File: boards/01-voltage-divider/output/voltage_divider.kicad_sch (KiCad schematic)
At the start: 4 parts, among them J1 IN, J2 OUT

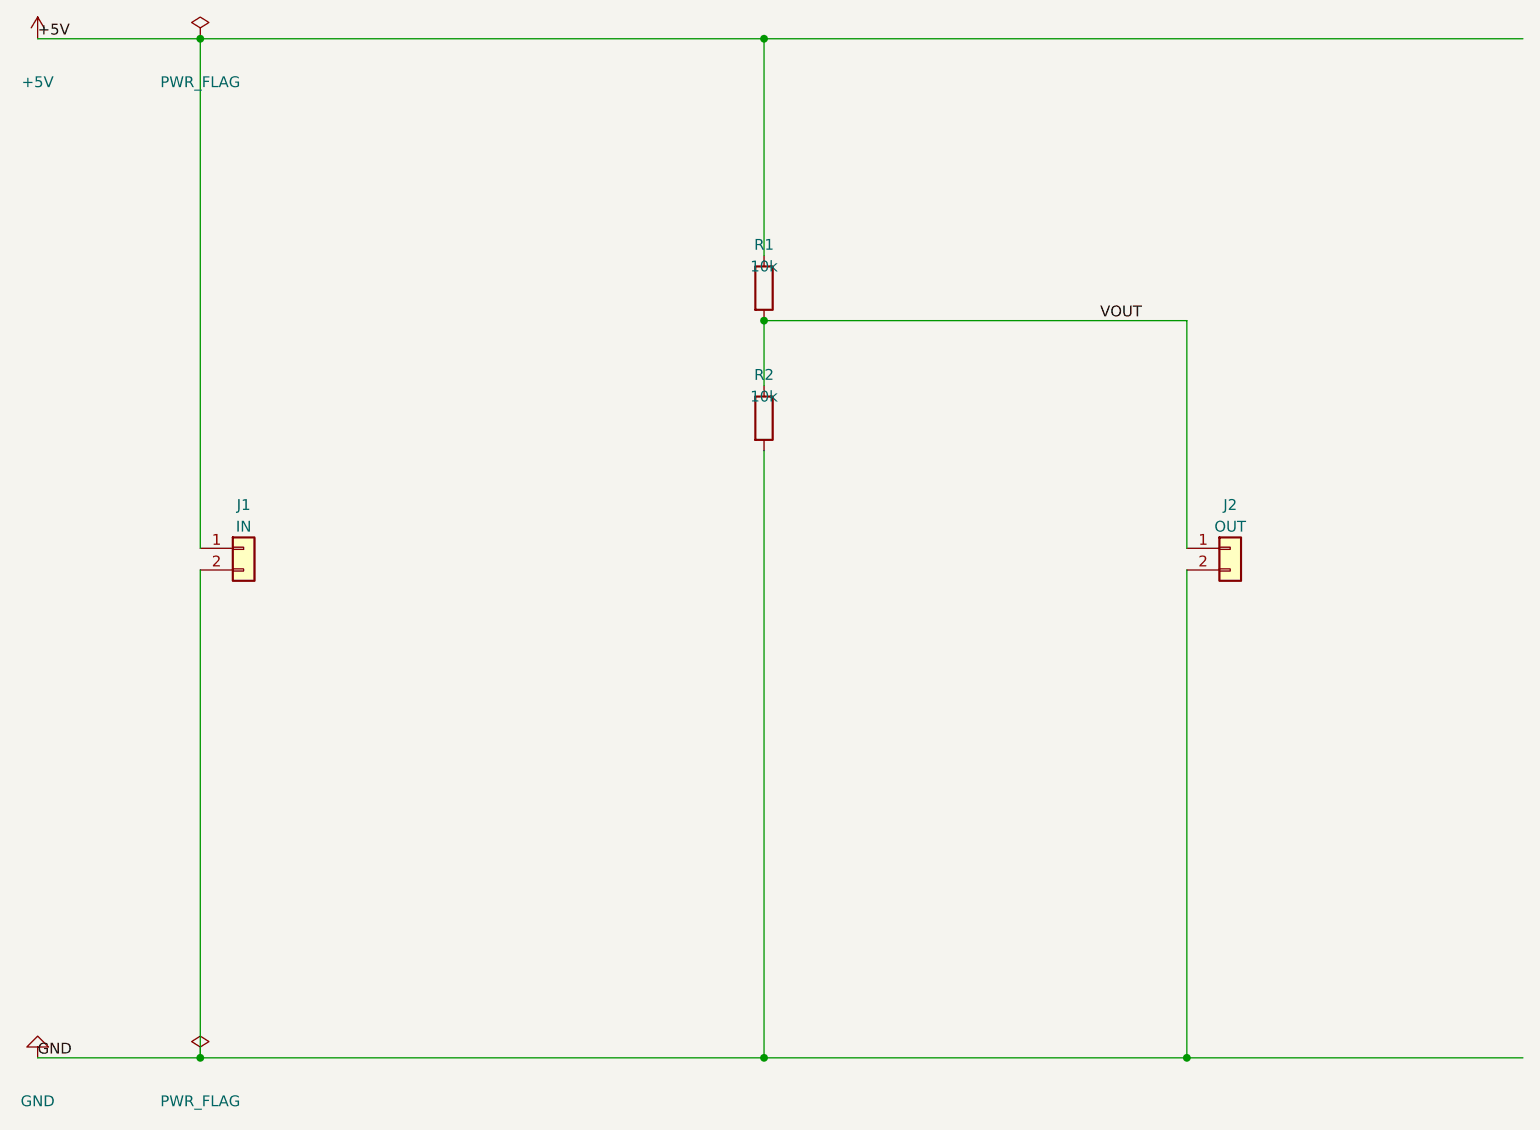
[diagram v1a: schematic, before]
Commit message: fix(boards): Add ERC validation to generate_design.py
The script previously reported SUCCESS even when the schematic had ERC
errors. Now runs KiCad ERC validation after schematic creation and:
- Reports ERC errors/warnings in the console output
- Includes ERC status in the summary (PASS/FAIL)
- Returns non-zero exit code when ERC errors are found
- Gracefully skips ERC if kicad-cli is not available

Co-Authored-By: Claude Opus 4.5 <noreply@anthropic.com>
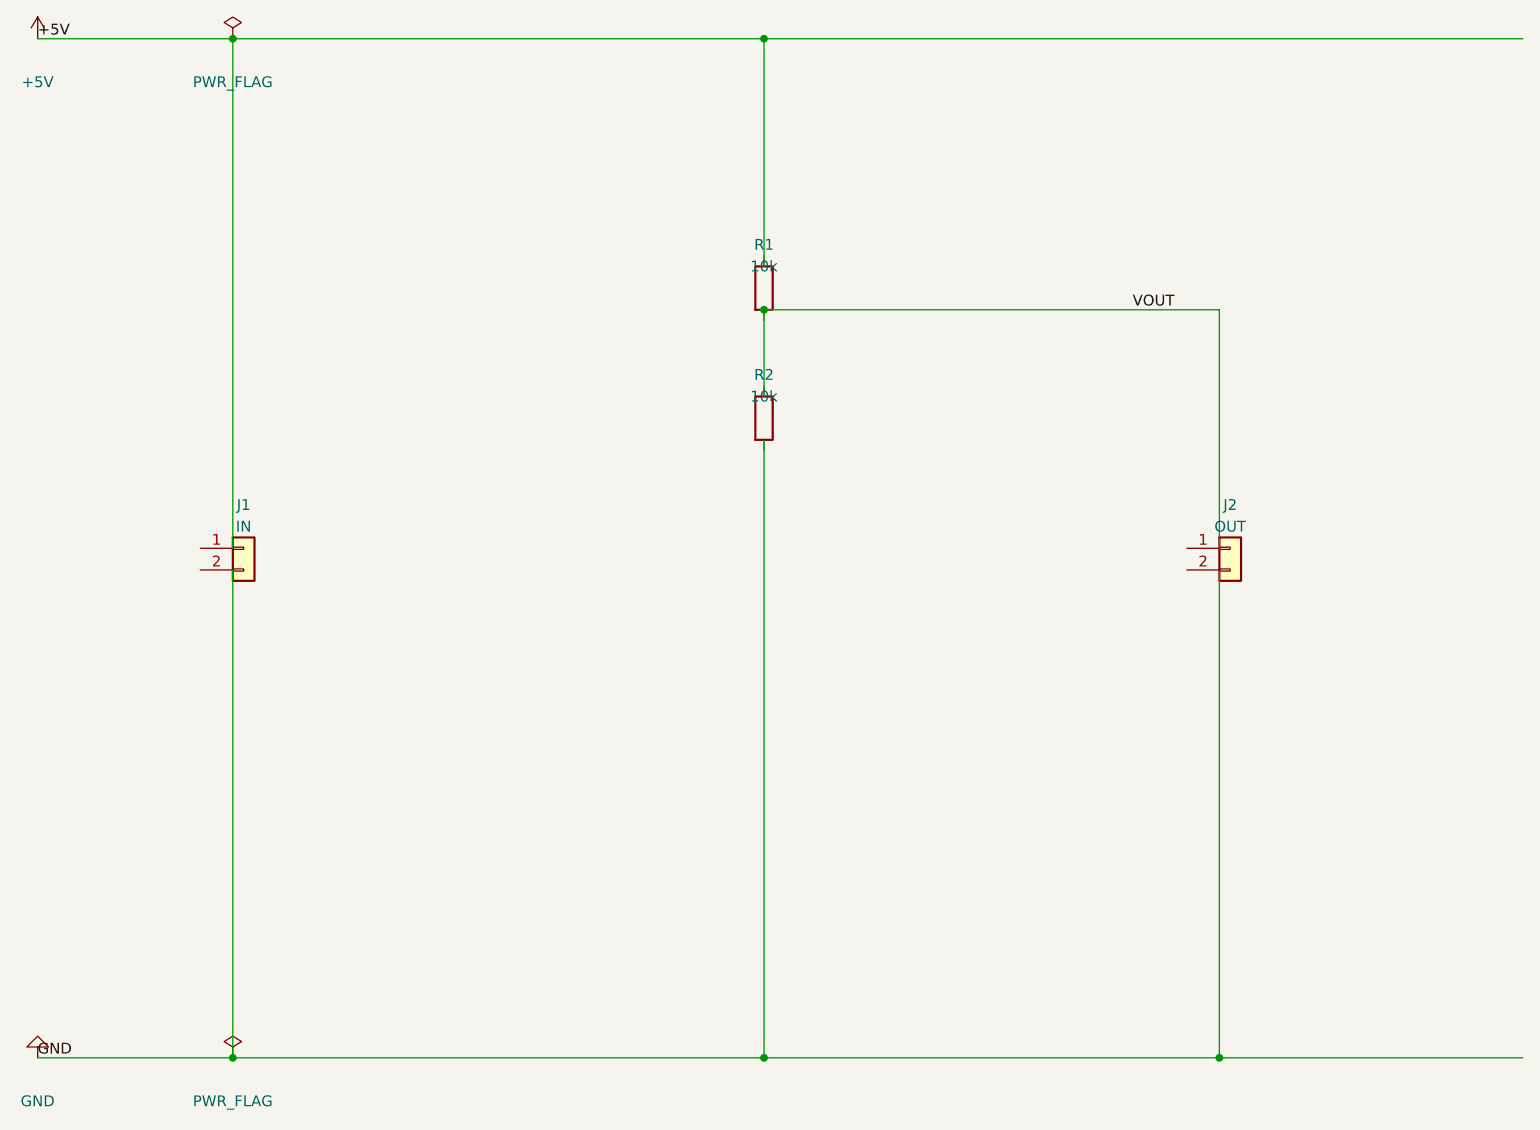
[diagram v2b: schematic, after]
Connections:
- net +5V: no longer J1.1 (Pin_1), R1.1
- net GND: no longer J1.2 (Pin_2), J2.2 (Pin_2), R2.2
- net VOUT: no longer J2.1 (Pin_1), R1.2, R2.1
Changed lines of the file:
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@@
     (instances
       (project "project"
-        (path "/9375341a-6719-4783-a821-5891f6b993f4" (reference "J1") (unit 1)
+        (path "/72230662-432b-4452-80bb-e7fa0bcafb7e" (reference "J1") (unit 1)
         )
       )
@@
     (instances
       (project "project"
-        (path "/9375341a-6719-4783-a821-5891f6b993f4" (reference "R1") (unit 1)
+        (path "/72230662-432b-4452-80bb-e7fa0bcafb7e" (reference "R1") (unit 1)
         )
       )
@@
     (instances
       (project "project"
-        (path "/9375341a-6719-4783-a821-5891f6b993f4" (reference "R2") (unit 1)
+        (path "/72230662-432b-4452-80bb-e7fa0bcafb7e" (reference "R2") (unit 1)
         )
       )
@@
     (instances
       (project "project"
-        (path "/9375341a-6719-4783-a821-5891f6b993f4" (reference "J2") (unit 1)
+        (path "/72230662-432b-4452-80bb-e7fa0bcafb7e" (reference "J2") (unit 1)
         )
       )
@@
     (instances
       (project "project"
-        (path "/9375341a-6719-4783-a821-5891f6b993f4" (reference "#PWR01") (unit 1)
+        (path "/72230662-432b-4452-80bb-e7fa0bcafb7e" (reference "#PWR01") (unit 1)
         )
       )
@@
     (instances
       (project "project"
-        (path "/9375341a-6719-4783-a821-5891f6b993f4" (reference "#PWR02") (unit 1)
+        (path "/72230662-432b-4452-80bb-e7fa0bcafb7e" (reference "#PWR02") (unit 1)
         )
       )
@@
   (symbol
     (lib_id "power:PWR_FLAG")
-    (at 44.45 30.48 0)
+    (at 48.26 30.48 0)
     (unit 1)
     (exclude_from_sim no)
@@
     (dnp no)
     (property "Reference" "#PWR03"
-      (at 44.45 33.02 0)
+      (at 48.26 33.02 0)
       (effects
         (font
@@
     )
     (property "Value" "PWR_FLAG"
-      (at 44.45 35.56 0)
-      (effects
-        (font
-          (size 1.27 1.27)
-        )
-      )
-    )
-    (property "Footprint" ""
-      (at 44.45 30.48 0)
+      (at 48.26 35.56 0)
+      (effects
+        (font
+          (size 1.27 1.27)
+        )
+      )
+    )
+    (property "Footprint" ""
+      (at 48.26 30.48 0)
       (effects
         (font
@@
     )
     (property "Datasheet" ""
-      (at 44.45 30.48 0)
-      (effects
-        (font
-          (size 1.27 1.27)
-        )
-        (hide yes)
-      )
-    )
-    (pin "1"
-    )
-    (instances
-      (project "project"
-        (path "/9375341a-6719-4783-a821-5891f6b993f4" (reference "#PWR03") (unit 1)
+      (at 48.26 30.48 0)
+      (effects
+        (font
+          (size 1.27 1.27)
+        )
+        (hide yes)
+      )
+    )
+    (pin "1"
+    )
+    (instances
+      (project "project"
+        (path "/72230662-432b-4452-80bb-e7fa0bcafb7e" (reference "#PWR03") (unit 1)
         )
       )
@@
   (symbol
     (lib_id "power:PWR_FLAG")
-    (at 44.45 149.86 0)
+    (at 48.26 149.86 0)
     (unit 1)
     (exclude_from_sim no)
@@
     (dnp no)
     (property "Reference" "#PWR04"
-      (at 44.45 152.4 0)
+      (at 48.26 152.4 0)
       (effects
         (font
@@
     )
     (property "Value" "PWR_FLAG"
-      (at 44.45 154.94 0)
-      (effects
-        (font
-          (size 1.27 1.27)
-        )
-      )
-    )
-    (property "Footprint" ""
-      (at 44.45 149.86 0)
+      (at 48.26 154.94 0)
+      (effects
+        (font
+          (size 1.27 1.27)
+        )
+      )
+    )
+    (property "Footprint" ""
+      (at 48.26 149.86 0)
       (effects
         (font
@@
     )
     (property "Datasheet" ""
-      (at 44.45 149.86 0)
-      (effects
-        (font
-          (size 1.27 1.27)
-        )
-        (hide yes)
-      )
-    )
-    (pin "1"
-    )
-    (instances
-      (project "project"
-        (path "/9375341a-6719-4783-a821-5891f6b993f4" (reference "#PWR04") (unit 1)
-        )
-      )
-    )
-  )
-  (wire
-    (pts (xy 25.4 30.48) (xy 44.45 30.48))
-    (stroke
-      (width 0)
-      (type default)
-    )
-  )
-  (wire
-    (pts (xy 44.45 30.48) (xy 110.49 30.48))
+      (at 48.26 149.86 0)
+      (effects
+        (font
+          (size 1.27 1.27)
+        )
+        (hide yes)
+      )
+    )
+    (pin "1"
+    )
+    (instances
+      (project "project"
+        (path "/72230662-432b-4452-80bb-e7fa0bcafb7e" (reference "#PWR04") (unit 1)
+        )
+      )
+    )
+  )
+  (wire
+    (pts (xy 25.4 30.48) (xy 48.26 30.48))
+    (stroke
+      (width 0)
+      (type default)
+    )
+  )
+  (wire
+    (pts (xy 48.26 30.48) (xy 110.49 30.48))
     (stroke
       (width 0)
@@
   )
   (wire
-    (pts (xy 25.4 149.86) (xy 44.45 149.86))
-    (stroke
-      (width 0)
-      (type default)
-    )
-  )
-  (wire
-    (pts (xy 44.45 149.86) (xy 110.49 149.86))
-    (stroke
-      (width 0)
-      (type default)
-    )
-  )
-  (wire
-    (pts (xy 110.49 149.86) (xy 160.02 149.86))
-    (stroke
-      (width 0)
-      (type default)
-    )
-  )
-  (wire
-    (pts (xy 160.02 149.86) (xy 199.39 149.86))
-    (stroke
-      (width 0)
-      (type default)
-    )
-  )
-  (wire
-    (pts (xy 44.45 90.17) (xy 44.45 30.48))
-    (stroke
-      (width 0)
-      (type default)
-    )
-  )
-  (wire
-    (pts (xy 44.45 92.71) (xy 44.45 149.86))
-    (stroke
-      (width 0)
-      (type default)
-    )
-  )
-  (wire
-    (pts (xy 110.49 55.88) (xy 110.49 30.48))
-    (stroke
-      (width 0)
-      (type default)
-    )
-  )
-  (wire
-    (pts (xy 110.49 63.5) (xy 110.49 71.12))
-    (stroke
-      (width 0)
-      (type default)
-    )
-  )
-  (wire
-    (pts (xy 110.49 78.74) (xy 110.49 149.86))
-    (stroke
-      (width 0)
-      (type default)
-    )
-  )
-  (wire
-    (pts (xy 110.49 63.5) (xy 160.02 63.5))
-    (stroke
-      (width 0)
-      (type default)
-    )
-  )
-  (wire
-    (pts (xy 160.02 63.5) (xy 160.02 90.17))
-    (stroke
-      (width 0)
-      (type default)
-    )
-  )
-  (wire
-    (pts (xy 160.02 92.71) (xy 160.02 149.86))
+    (pts (xy 25.4 149.86) (xy 48.26 149.86))
+    (stroke
+      (width 0)
+      (type default)
+    )
+  )
+  (wire
+    (pts (xy 48.26 149.86) (xy 110.49 149.86))
+    (stroke
+      (width 0)
+      (type default)
+    )
+  )
+  (wire
+    (pts (xy 110.49 149.86) (xy 163.83 149.86))
+    (stroke
+      (width 0)
+      (type default)
+    )
+  )
+  (wire
+    (pts (xy 163.83 149.86) (xy 199.39 149.86))
+    (stroke
+      (width 0)
+      (type default)
+    )
+  )
+  (wire
+    (pts (xy 48.26 90.17) (xy 48.26 30.48))
+    (stroke
+      (width 0)
+      (type default)
+    )
+  )
+  (wire
+    (pts (xy 48.26 92.71) (xy 48.26 149.86))
+    (stroke
+      (width 0)
+      (type default)
+    )
+  )
+  (wire
+    (pts (xy 110.49 57.15) (xy 110.49 30.48))
+    (stroke
+      (width 0)
+      (type default)
+    )
+  )
+  (wire
+    (pts (xy 110.49 62.23) (xy 110.49 72.39))
+    (stroke
+      (width 0)
+      (type default)
+    )
+  )
+  (wire
+    (pts (xy 110.49 77.47) (xy 110.49 149.86))
+    (stroke
+      (width 0)
+      (type default)
+    )
+  )
+  (wire
+    (pts (xy 110.49 62.23) (xy 163.83 62.23))
+    (stroke
+      (width 0)
+      (type default)
+    )
+  )
+  (wire
+    (pts (xy 163.83 62.23) (xy 163.83 90.17))
+    (stroke
+      (width 0)
+      (type default)
+    )
+  )
+  (wire
+    (pts (xy 163.83 92.71) (xy 163.83 149.86))
     (stroke
       (width 0)
@@
   )
   (junction
-    (at 44.45 30.48)
+    (at 48.26 30.48)
     (diameter 0)
   )
   (junction
-    (at 44.45 149.86)
+    (at 48.26 149.86)
     (diameter 0)
   )
@@
   )
   (junction
-    (at 110.49 63.5)
+    (at 110.49 62.23)
     (diameter 0)
   )
@@
   )
   (junction
-    (at 160.02 149.86)
+    (at 163.83 149.86)
     (diameter 0)
   )
@@
   )
   (label "VOUT"
-    (at 149.86 63.5 0)
+    (at 153.67 62.23 0)
     (fields_autoplaced yes)
     (effects
@@
   )
   (sheet_instances
-    (path "/9375341a-6719-4783-a821-5891f6b993f4" (page "1")
-    )
-  )
+    (path "/72230662-432b-4452-80bb-e7fa0bcafb7e" (page "1")
+    )
+  )

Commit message: fix(examples): Add footprint assignments to schematic examples (#678)
Update the charlieplex and voltage divider example scripts to use the
existing `footprint` and `auto_footprint` parameters in add_symbol().

Changes:
- charlieplex: Add explicit footprint for MCU connector, auto_footprint
  for resistors, and explicit footprints for LEDs
- voltage_divider: Add explicit footprints for connectors and
  auto_footprint for resistors
- Regenerated output files with footprint assignments

The `footprint` parameter and `auto_footprint` feature already existed
in add_symbol() - the examples just weren't using them, which caused
"Missing footprint" warnings during schematic validation.

Closes #678

Co-Authored-By: Claude Opus 4.5 <noreply@anthropic.com>
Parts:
- J1, J2: footprint (none) -> Connector_PinHeader_2.54mm:PinHeader_1x02_P2.54mm_Vertical
- R1, R2: footprint (none) -> Resistor_SMD:R_0402_1005Metric
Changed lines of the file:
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@@
       )
     )
-    (property "Footprint" ""
+    (property "Footprint" "Connector_PinHeader_2.54mm:PinHeader_1x02_P2.54mm_Vertical"
       (at 49.53 90.17 0)
       (effects
@@
     (instances
       (project "project"
-        (path "/72230662-432b-4452-80bb-e7fa0bcafb7e" (reference "J1") (unit 1)
+        (path "/f6577161-ce3c-4d5c-9281-2bb1198b1d2d" (reference "J1") (unit 1)
         )
       )
@@
       )
     )
-    (property "Footprint" ""
+    (property "Footprint" "Resistor_SMD:R_0402_1005Metric"
       (at 110.49 59.69 0)
       (effects
@@
     (instances
       (project "project"
-        (path "/72230662-432b-4452-80bb-e7fa0bcafb7e" (reference "R1") (unit 1)
+        (path "/f6577161-ce3c-4d5c-9281-2bb1198b1d2d" (reference "R1") (unit 1)
         )
       )
@@
       )
     )
-    (property "Footprint" ""
+    (property "Footprint" "Resistor_SMD:R_0402_1005Metric"
       (at 110.49 74.93 0)
       (effects
@@
     (instances
       (project "project"
-        (path "/72230662-432b-4452-80bb-e7fa0bcafb7e" (reference "R2") (unit 1)
+        (path "/f6577161-ce3c-4d5c-9281-2bb1198b1d2d" (reference "R2") (unit 1)
         )
       )
@@
       )
     )
-    (property "Footprint" ""
+    (property "Footprint" "Connector_PinHeader_2.54mm:PinHeader_1x02_P2.54mm_Vertical"
       (at 165.1 90.17 0)
       (effects
@@
     (instances
       (project "project"
-        (path "/72230662-432b-4452-80bb-e7fa0bcafb7e" (reference "J2") (unit 1)
+        (path "/f6577161-ce3c-4d5c-9281-2bb1198b1d2d" (reference "J2") (unit 1)
         )
       )
@@
     (instances
       (project "project"
-        (path "/72230662-432b-4452-80bb-e7fa0bcafb7e" (reference "#PWR01") (unit 1)
+        (path "/f6577161-ce3c-4d5c-9281-2bb1198b1d2d" (reference "#PWR01") (unit 1)
         )
       )
@@
     (instances
       (project "project"
-        (path "/72230662-432b-4452-80bb-e7fa0bcafb7e" (reference "#PWR02") (unit 1)
+        (path "/f6577161-ce3c-4d5c-9281-2bb1198b1d2d" (reference "#PWR02") (unit 1)
         )
       )
@@
     (instances
       (project "project"
-        (path "/72230662-432b-4452-80bb-e7fa0bcafb7e" (reference "#PWR03") (unit 1)
+        (path "/f6577161-ce3c-4d5c-9281-2bb1198b1d2d" (reference "#PWR03") (unit 1)
         )
       )
@@
     (instances
       (project "project"
-        (path "/72230662-432b-4452-80bb-e7fa0bcafb7e" (reference "#PWR04") (unit 1)
+        (path "/f6577161-ce3c-4d5c-9281-2bb1198b1d2d" (reference "#PWR04") (unit 1)
         )
       )
@@
   )
   (sheet_instances
-    (path "/72230662-432b-4452-80bb-e7fa0bcafb7e" (page "1")
-    )
-  )
+    (path "/f6577161-ce3c-4d5c-9281-2bb1198b1d2d" (page "1")
+    )
+  )
